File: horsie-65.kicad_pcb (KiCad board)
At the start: 2 copper layers, 304.8 x 95.3 mm, 30 parts, among them SW14 BSPC, SW16 TAB, SW29 \|, SW31 CAPS, SW42 ', SW43 ENTR, SW44 PGUP, SW45 LSHF, SW46 Z, SW47 X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

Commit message: isolate clock
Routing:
- net +5V: track 182.6 -> 188.1 mm
- net GND: track 199.8 -> 203.7 mm
- net XTAL2: track 14.1 -> 17.6 mm
- net XTAL1: track 16.4 -> 19.2 mm
- net col10: track 144.3 -> 146.4 mm
- net col9: track 126.1 -> 127.8 mm
- net col11: track 158.7 -> 157.6 mm

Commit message: minor stuff
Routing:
- net col8: track 117.9 -> 120.7 mm
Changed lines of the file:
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@@
     (thickness 1.6)
     (drawings 8)
-    (tracks 1238)
+    (tracks 1239)
     (zones 0)
     (modules 151)
@@
   (segment (start 196.215 68.8975) (end 196.215 70.231) (width 0.254) (layer F.Cu) (net 95))
   (segment (start 196.215 70.231) (end 196.85 70.866) (width 0.254) (layer F.Cu) (net 95))
-  (segment (start 207.137 101.6) (end 207.137 106.80701) (width 0.254) (layer F.Cu) (net 95))
   (via (at 201.168 112.77601) (size 0.8) (drill 0.4) (layers F.Cu B.Cu) (net 95))
-  (segment (start 207.137 106.80701) (end 201.567999 112.376011) (width 0.254) (layer F.Cu) (net 95))
-  (segment (start 201.567999 112.376011) (end 201.168 112.77601) (width 0.254) (layer F.Cu) (net 95))
-  (segment (start 205.74 87.9475) (end 205.74 100.203) (width 0.254) (layer F.Cu) (net 95))
-  (segment (start 205.74 100.203) (end 207.137 101.6) (width 0.254) (layer F.Cu) (net 95))
   (segment (start 200.40599 112.77601) (end 201.168 112.77601) (width 0.254) (layer B.Cu) (net 95))
   (segment (start 198.374 114.808) (end 200.40599 112.77601) (width 0.254) (layer B.Cu) (net 95))
@@
   (segment (start 181.9125 107.9625) (end 182.8925 107.9625) (width 0.254) (layer B.Cu) (net 95))
   (segment (start 182.8925 107.9625) (end 189.738 114.808) (width 0.254) (layer B.Cu) (net 95))
+  (segment (start 201.567999 112.376011) (end 201.168 112.77601) (width 0.254) (layer F.Cu) (net 95))
+  (segment (start 206.393989 112.376011) (end 201.567999 112.376011) (width 0.254) (layer F.Cu) (net 95))
+  (segment (start 207.137 101.6) (end 207.137 111.633) (width 0.254) (layer F.Cu) (net 95))
+  (segment (start 205.74 87.9475) (end 205.74 100.203) (width 0.254) (layer F.Cu) (net 95))
+  (segment (start 205.74 100.203) (end 207.137 101.6) (width 0.254) (layer F.Cu) (net 95))
+  (segment (start 207.137 111.633) (end 206.393989 112.376011) (width 0.254) (layer F.Cu) (net 95))
   (segment (start 201.6125 40.9575) (end 210.5025 49.8475) (width 0.254) (layer F.Cu) (net 96))
   (segment (start 201.6125 32.7025) (end 201.6125 40.9575) (width 0.254) (layer F.Cu) (net 96))
@@
   (segment (start 200.152 113.792) (end 200.659994 113.792) (width 0.254) (layer B.Cu) (net 96))
   (segment (start 181.9125 108.7625) (end 182.9305 108.7625) (width 0.254) (layer B.Cu) (net 96))
-  (segment (start 201.227962 113.792) (end 201.225679 113.792) (width 0.254) (layer F.Cu) (net 96))
-  (segment (start 224.79 94.615) (end 206.629 112.776) (width 0.254) (layer F.Cu) (net 96))
-  (segment (start 202.243962 112.776) (end 201.227962 113.792) (width 0.254) (layer F.Cu) (net 96))
-  (segment (start 206.629 112.776) (end 202.243962 112.776) (width 0.254) (layer F.Cu) (net 96))
-  (segment (start 224.79 87.9475) (end 224.79 94.615) (width 0.254) (layer F.Cu) (net 96))
+  (segment (start 202.18994 112.830022) (end 201.227962 113.792) (width 0.254) (layer F.Cu) (net 96))
   (segment (start 201.225679 113.792) (end 200.659994 113.792) (width 0.254) (layer F.Cu) (net 96))
+  (segment (start 201.227962 113.792) (end 201.225679 113.792) (width 0.254) (layer F.Cu) (net 96))
+  (segment (start 224.79 87.9475) (end 224.79 94.622068) (width 0.254) (layer F.Cu) (net 96))
+  (segment (start 206.582046 112.830022) (end 202.18994 112.830022) (width 0.254) (layer F.Cu) (net 96))
+  (segment (start 224.79 94.622068) (end 206.582046 112.830022) (width 0.254) (layer F.Cu) (net 96))
   (segment (start 220.6625 40.9575) (end 229.5525 49.8475) (width 0.254) (layer F.Cu) (net 97))
   (segment (start 220.6625 32.7025) (end 220.6625 40.9575) (width 0.254) (layer F.Cu) (net 97))
@@
   (segment (start 243.84 89.535) (end 243.84 87.9475) (width 0.254) (layer F.Cu) (net 97))
   (via (at 200.158071 114.814077) (size 0.8) (drill 0.4) (layers F.Cu B.Cu) (net 97))
-  (segment (start 202.37803 113.284) (end 200.847953 114.814077) (width 0.254) (layer F.Cu) (net 97))
-  (segment (start 222.40875 106.9975) (end 213.049568 106.9975) (width 0.254) (layer F.Cu) (net 97))
-  (segment (start 206.763068 113.284) (end 202.37803 113.284) (width 0.254) (layer F.Cu) (net 97))
-  (segment (start 200.723756 114.814077) (end 200.158071 114.814077) (width 0.254) (layer F.Cu) (net 97))
-  (segment (start 213.049568 106.9975) (end 206.763068 113.284) (width 0.254) (layer F.Cu) (net 97))
-  (segment (start 200.847953 114.814077) (end 200.723756 114.814077) (width 0.254) (layer F.Cu) (net 97))
   (segment (start 199.771991 114.814077) (end 200.158071 114.814077) (width 0.254) (layer B.Cu) (net 97))
   (segment (start 198.762068 115.824) (end 199.771991 114.814077) (width 0.254) (layer B.Cu) (net 97))
@@
   (segment (start 181.9125 109.5625) (end 182.9165 109.5625) (width 0.254) (layer B.Cu) (net 97))
   (segment (start 182.9165 109.5625) (end 189.178 115.824) (width 0.254) (layer B.Cu) (net 97))
+  (segment (start 222.40875 106.9975) (end 213.056636 106.9975) (width 0.254) (layer F.Cu) (net 97))
+  (segment (start 213.056636 106.9975) (end 206.770103 113.284033) (width 0.254) (layer F.Cu) (net 97))
+  (segment (start 200.847953 114.814077) (end 200.723756 114.814077) (width 0.254) (layer F.Cu) (net 97))
+  (segment (start 200.723756 114.814077) (end 200.158071 114.814077) (width 0.254) (layer F.Cu) (net 97))
+  (segment (start 202.377997 113.284033) (end 200.847953 114.814077) (width 0.254) (layer F.Cu) (net 97))
+  (segment (start 206.770103 113.284033) (end 202.377997 113.284033) (width 0.254) (layer F.Cu) (net 97))
   (segment (start 239.7125 40.9575) (end 248.6025 49.8475) (width 0.254) (layer F.Cu) (net 98))
   (segment (start 239.7125 32.7025) (end 239.7125 40.9575) (width 0.254) (layer F.Cu) (net 98))

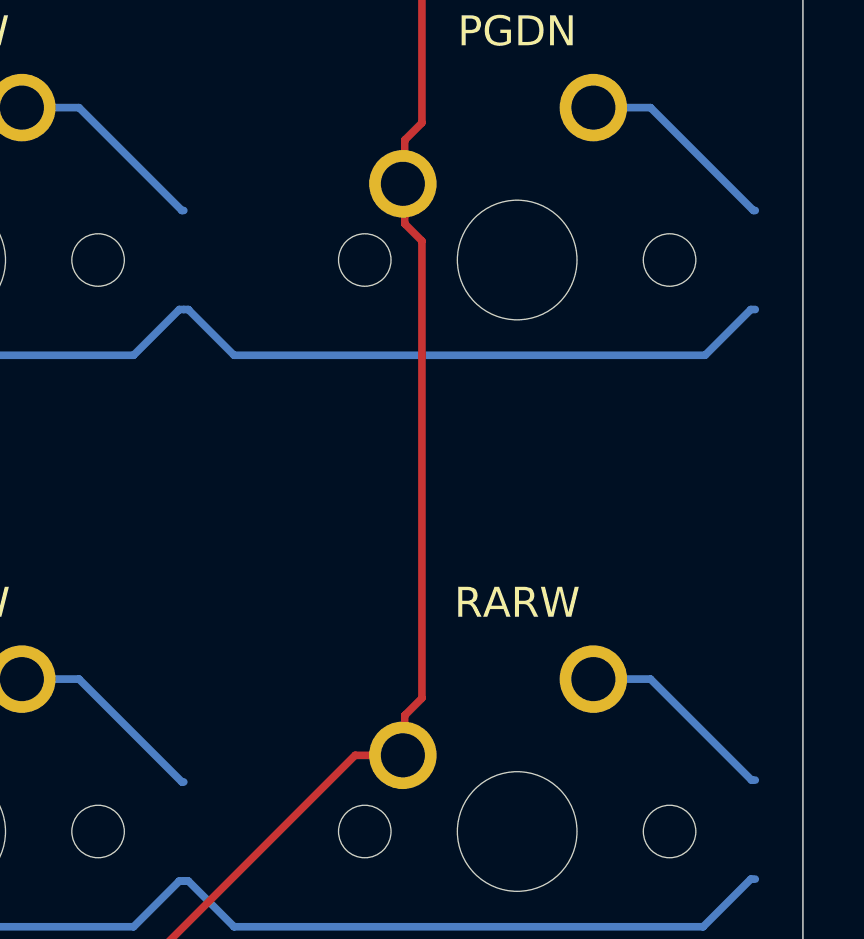
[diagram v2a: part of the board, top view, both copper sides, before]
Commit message: ground fill fix
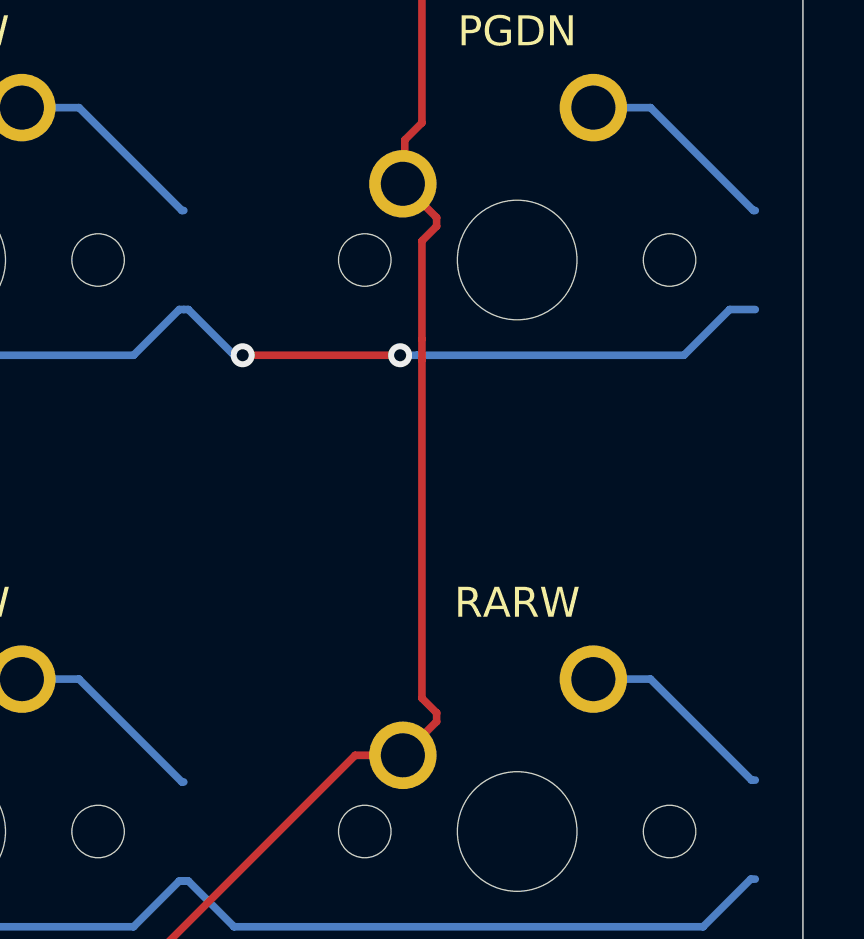
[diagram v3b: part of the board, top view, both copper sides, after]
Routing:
- net col14: track 225.1 -> 225.9 mm
- net row3: vias 0 -> 2
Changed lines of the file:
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@@
     (thickness 1.6)
     (drawings 8)
-    (tracks 1239)
+    (tracks 1248)
     (zones 0)
     (modules 151)
@@
   (segment (start 53.975 92.1375) (end 54.125 92.1375) (width 0.254) (layer B.Cu) (net 54))
   (segment (start 54.125 92.1375) (end 55.65 93.6625) (width 0.254) (layer B.Cu) (net 54))
-  (segment (start 308.125 92.1375) (end 307.975 92.1375) (width 0.254) (layer B.Cu) (net 54))
-  (segment (start 309.65 93.6625) (end 308.125 92.1375) (width 0.254) (layer B.Cu) (net 54))
-  (segment (start 325.35 93.6625) (end 309.65 93.6625) (width 0.254) (layer B.Cu) (net 54))
-  (segment (start 327.025 92.1375) (end 326.875 92.1375) (width 0.254) (layer B.Cu) (net 54))
-  (segment (start 326.875 92.1375) (end 325.35 93.6625) (width 0.254) (layer B.Cu) (net 54))
   (segment (start 281.93125 92.1375) (end 281.78125 92.1375) (width 0.254) (layer B.Cu) (net 54))
   (segment (start 283.45625 93.6625) (end 281.93125 92.1375) (width 0.254) (layer B.Cu) (net 54))
@@
   (segment (start 217.4875 92.2) (end 217.3375 92.2) (width 0.254) (layer B.Cu) (net 54))
   (segment (start 217.3375 92.2) (end 215.875 93.6625) (width 0.254) (layer B.Cu) (net 54))
+  (via (at 315.185506 93.6625) (size 0.8) (drill 0.4) (layers F.Cu B.Cu) (net 54))
+  (segment (start 324.646 93.6625) (end 315.751191 93.6625) (width 0.254) (layer B.Cu) (net 54))
+  (segment (start 326.171 92.1375) (end 324.646 93.6625) (width 0.254) (layer B.Cu) (net 54))
+  (segment (start 315.751191 93.6625) (end 315.185506 93.6625) (width 0.254) (layer B.Cu) (net 54))
+  (segment (start 327.025 92.1375) (end 326.171 92.1375) (width 0.254) (layer B.Cu) (net 54))
+  (via (at 309.937703 93.6625) (size 0.8) (drill 0.4) (layers F.Cu B.Cu) (net 54))
+  (segment (start 315.185506 93.6625) (end 309.937703 93.6625) (width 0.254) (layer F.Cu) (net 54))
+  (segment (start 307.975 92.1375) (end 308.125 92.1375) (width 0.254) (layer B.Cu) (net 54))
+  (segment (start 308.125 92.1375) (end 309.65 93.6625) (width 0.254) (layer B.Cu) (net 54))
+  (segment (start 309.65 93.6625) (end 309.937703 93.6625) (width 0.254) (layer B.Cu) (net 54))
   (segment (start 84.075 88.8375) (end 84.1375 88.8375) (width 0.254) (layer B.Cu) (net 55))
   (segment (start 78.74 85.4075) (end 80.645 85.4075) (width 0.254) (layer B.Cu) (net 55))
@@
   (segment (start 315.2775 68.8975) (end 315.2775 70.2945) (width 0.254) (layer F.Cu) (net 101))
   (segment (start 315.2775 70.2945) (end 315.9125 70.9295) (width 0.254) (layer F.Cu) (net 101))
-  (segment (start 315.341 106.934) (end 315.2775 106.9975) (width 0.254) (layer F.Cu) (net 101))
-  (segment (start 315.2775 87.9475) (end 315.341 88.011) (width 0.254) (layer F.Cu) (net 101))
-  (segment (start 315.341 89.281) (end 315.9125 89.8525) (width 0.254) (layer F.Cu) (net 101))
-  (segment (start 315.341 88.011) (end 315.341 89.281) (width 0.254) (layer F.Cu) (net 101))
-  (segment (start 315.9125 89.8525) (end 315.9125 105.0925) (width 0.254) (layer F.Cu) (net 101))
-  (segment (start 315.9125 105.0925) (end 315.341 105.664) (width 0.254) (layer F.Cu) (net 101))
-  (segment (start 315.341 105.664) (end 315.341 106.934) (width 0.254) (layer F.Cu) (net 101))
   (via (at 182.824731 117.983466) (size 0.8) (drill 0.4) (layers F.Cu B.Cu) (net 101))
   (segment (start 177.0125 112.0625) (end 177.0125 114.4015) (width 0.254) (layer B.Cu) (net 101))
@@
   (segment (start 203.041302 115.189) (end 200.246836 117.983466) (width 0.254) (layer F.Cu) (net 101))
   (segment (start 313.68651 106.9975) (end 305.49501 115.189) (width 0.254) (layer F.Cu) (net 101))
+  (segment (start 315.9125 93.12303) (end 315.912508 93.123038) (width 0.254) (layer F.Cu) (net 101))
+  (segment (start 315.912508 93.123038) (end 315.912508 93.820962) (width 0.254) (layer F.Cu) (net 101))
+  (segment (start 315.9125 93.82097) (end 315.9125 105.0925) (width 0.254) (layer F.Cu) (net 101))
+  (segment (start 316.402499 105.872501) (end 315.2775 106.9975) (width 0.254) (layer F.Cu) (net 101))
+  (segment (start 315.9125 89.8525) (end 315.9125 93.12303) (width 0.254) (layer F.Cu) (net 101))
+  (segment (start 316.402499 105.582499) (end 316.402499 105.872501) (width 0.254) (layer F.Cu) (net 101))
+  (segment (start 315.9125 105.0925) (end 316.402499 105.582499) (width 0.254) (layer F.Cu) (net 101))
+  (segment (start 316.402499 89.072499) (end 316.402499 89.362501) (width 0.254) (layer F.Cu) (net 101))
+  (segment (start 316.402499 89.362501) (end 315.9125 89.8525) (width 0.254) (layer F.Cu) (net 101))
+  (segment (start 315.2775 87.9475) (end 316.402499 89.072499) (width 0.254) (layer F.Cu) (net 101))
+  (segment (start 315.912508 93.820962) (end 315.9125 93.82097) (width 0.254) (layer F.Cu) (net 101))
 )

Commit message: bruhhh
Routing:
- net row2: track 454.8 -> 454.9 mm, vias 0 -> 2
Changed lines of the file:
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@@
     (thickness 1.6)
     (drawings 8)
-    (tracks 1248)
+    (tracks 1252)
     (zones 0)
     (modules 151)
@@
   (segment (start 74.7625 73.0875) (end 76.2875 74.6125) (width 0.254) (layer B.Cu) (net 39))
   (segment (start 296.21875 73.0875) (end 296.06875 73.0875) (width 0.254) (layer B.Cu) (net 39))
-  (segment (start 297.74375 74.6125) (end 296.21875 73.0875) (width 0.254) (layer B.Cu) (net 39))
-  (segment (start 324.646 74.6125) (end 297.74375 74.6125) (width 0.254) (layer B.Cu) (net 39))
   (segment (start 327.025 73.0875) (end 326.171 73.0875) (width 0.254) (layer B.Cu) (net 39))
   (segment (start 326.171 73.0875) (end 324.646 74.6125) (width 0.254) (layer B.Cu) (net 39))
@@
   (segment (start 42.131288 94.234) (end 154.936462 94.234) (width 0.254) (layer B.Cu) (net 39))
   (segment (start 154.936462 94.234) (end 165.464962 104.7625) (width 0.254) (layer B.Cu) (net 39))
+  (via (at 297.65625 74.6125) (size 0.8) (drill 0.4) (layers F.Cu B.Cu) (net 39))
+  (segment (start 296.06875 73.0875) (end 296.13125 73.0875) (width 0.254) (layer B.Cu) (net 39))
+  (segment (start 296.13125 73.0875) (end 297.65625 74.6125) (width 0.254) (layer B.Cu) (net 39))
+  (via (at 315.11875 74.6125) (size 0.8) (drill 0.4) (layers F.Cu B.Cu) (net 39))
+  (segment (start 297.65625 74.6125) (end 315.11875 74.6125) (width 0.254) (layer F.Cu) (net 39))
+  (segment (start 315.11875 74.6125) (end 324.64375 74.6125) (width 0.254) (layer B.Cu) (net 39))
   (segment (start 74.55 69.7875) (end 74.6125 69.7875) (width 0.254) (layer B.Cu) (net 40))
   (segment (start 69.215 66.3575) (end 71.12 66.3575) (width 0.254) (layer B.Cu) (net 40))

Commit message: ground fill
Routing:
- net row4: track 312.9 -> 313.2 mm, vias 2 -> 4
- added copper zone on B.Cu, net GND
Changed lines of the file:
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@@
     (thickness 1.6)
     (drawings 8)
-    (tracks 1252)
+    (tracks 1255)
     (zones 0)
     (modules 151)
@@
   (segment (start 289.075 111.1875) (end 290.6 112.7125) (width 0.254) (layer B.Cu) (net 69))
   (segment (start 308.125 111.1875) (end 307.975 111.1875) (width 0.254) (layer B.Cu) (net 69))
-  (segment (start 309.65 112.7125) (end 308.125 111.1875) (width 0.254) (layer B.Cu) (net 69))
-  (segment (start 325.2875 112.7125) (end 309.65 112.7125) (width 0.254) (layer B.Cu) (net 69))
   (segment (start 327.025 111.125) (end 326.875 111.125) (width 0.254) (layer B.Cu) (net 69))
-  (segment (start 326.875 111.125) (end 325.2875 112.7125) (width 0.254) (layer B.Cu) (net 69))
   (segment (start 68.1125 111.1875) (end 68.2625 111.1875) (width 0.254) (layer B.Cu) (net 69))
   (segment (start 66.5875 112.7125) (end 68.1125 111.1875) (width 0.254) (layer B.Cu) (net 69))
@@
   (segment (start 164.211 112.395) (end 164.211 112.268) (width 0.254) (layer B.Cu) (net 69))
   (segment (start 164.211 112.268) (end 163.1305 111.1875) (width 0.254) (layer B.Cu) (net 69))
+  (via (at 309.5625 112.7125) (size 0.8) (drill 0.4) (layers F.Cu B.Cu) (net 69))
+  (segment (start 307.975 111.1875) (end 308.0375 111.1875) (width 0.254) (layer B.Cu) (net 69))
+  (segment (start 308.0375 111.1875) (end 309.5625 112.7125) (width 0.254) (layer B.Cu) (net 69))
+  (via (at 325.4375 112.7125) (size 0.8) (drill 0.4) (layers F.Cu B.Cu) (net 69))
+  (segment (start 309.5625 112.7125) (end 325.4375 112.7125) (width 0.254) (layer F.Cu) (net 69))
+  (segment (start 325.4375 112.7125) (end 327.025 111.125) (width 0.254) (layer B.Cu) (net 69))
   (segment (start 68.2 107.8875) (end 68.2625 107.8875) (width 0.254) (layer B.Cu) (net 70))
   (segment (start 62.07125 104.4575) (end 64.77 104.4575) (width 0.254) (layer B.Cu) (net 70))
@@
   (segment (start 315.2775 87.9475) (end 316.402499 89.072499) (width 0.254) (layer F.Cu) (net 101))
   (segment (start 315.912508 93.820962) (end 315.9125 93.82097) (width 0.254) (layer F.Cu) (net 101))
+  (zone (net 1) (net_name GND) (layer B.Cu) (hatch edge 0.508)
+    (connect_pads (clearance 0.508))
+    (min_thickness 0.254)
+    (fill yes (arc_segments 32) (thermal_gap 0.508) (thermal_bridge_width 0.508))
+    (polygon
+      (pts
+        (xy 23.01875 23.01875) (xy 329.40625 23.01875) (xy 329.40625 119.85625) (xy 23.01875 119.85625)
+      )
+    )
+  )
 )

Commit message: flip spcb
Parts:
- moved SW51 79.2 mm to (205.6, 161.9)
- moved SW56 79.2 mm to (308.0, 161.9)
- moved SW58 79.2 mm to (353.2, 161.9)
- moved SW14 79.2 mm to (324.6, 104.8)
- moved SW29 79.2 mm to (329.4, 123.8)
- moved SW44 79.2 mm to (353.2, 142.9)
- moved SW45 79.2 mm to (79.4, 161.9)
- moved SW46 79.2 mm to (110.3, 161.9)
- moved SW47 79.2 mm to (129.4, 161.9)
- moved SW48 79.2 mm to (148.4, 161.9)
- moved SW49 79.2 mm to (167.5, 161.9)
- moved SW50 79.2 mm to (186.5, 161.9)
- moved SW52 79.2 mm to (224.6, 161.9)
- moved SW53 79.2 mm to (243.7, 161.9)
- moved SW54 79.2 mm to (262.7, 161.9)
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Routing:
- net col8: track 120.7 -> 118.0 mm
- net col3: track 160.3 -> 159.0 mm
- net col0: track 242.6 -> 241.6 mm
- net col1: track 227.3 -> 226.4 mm
- net col11: track 157.6 -> 156.8 mm
- net row4: track 313.2 -> 313.7 mm
- net row3: track 308.4 -> 308.5 mm, vias 2 -> 4
- removed copper zone on B.Cu, net GND
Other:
- board size 304.8 x 95.3 mm -> 304.8 x 95.2 mm
